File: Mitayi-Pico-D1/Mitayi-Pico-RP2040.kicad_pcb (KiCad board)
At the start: 2 copper layers, 51 x 21 mm, 73 parts, among them J1 EXP8, J10 GND, J2 USB-C-2.0, J3 Header-1, J4 Header-2, J5 SWD, J7 VBUS, J8 DM, J9 DP, SW1 UK-B0273-SP25Y, SW2 UK-B0273-SP25Y, U1 W25Q32JVSSIQ, U2 MIC5219-3.3YM5, U3 RP2040, Y1 YIC-12M20P2/XT324-10/10

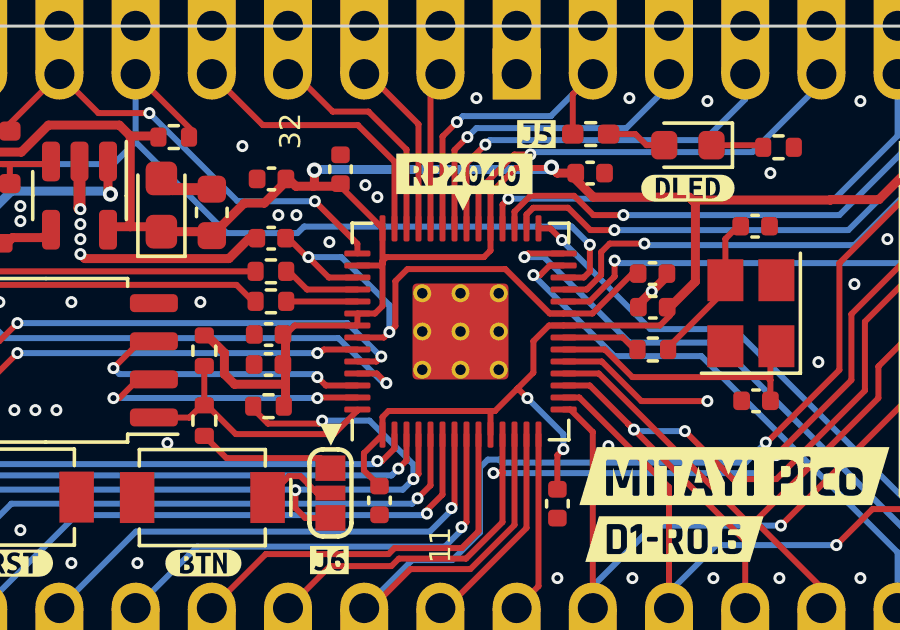
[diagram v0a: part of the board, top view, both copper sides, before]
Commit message: Updated `runDRC()`
- Updated `runDRC()`.
  - It now checks how many voilations were found in the DRC report and print them.
  - If violations are found, the user will be prompted to continue or exit the app.
  - The export log won't be saved if the user chooses to exit. The report will still be saved.
  - `pcb_drc` command execcution will be set to false if the user chooses to continue with DRC errors.
- New Version 🆕 `0.1.7`.
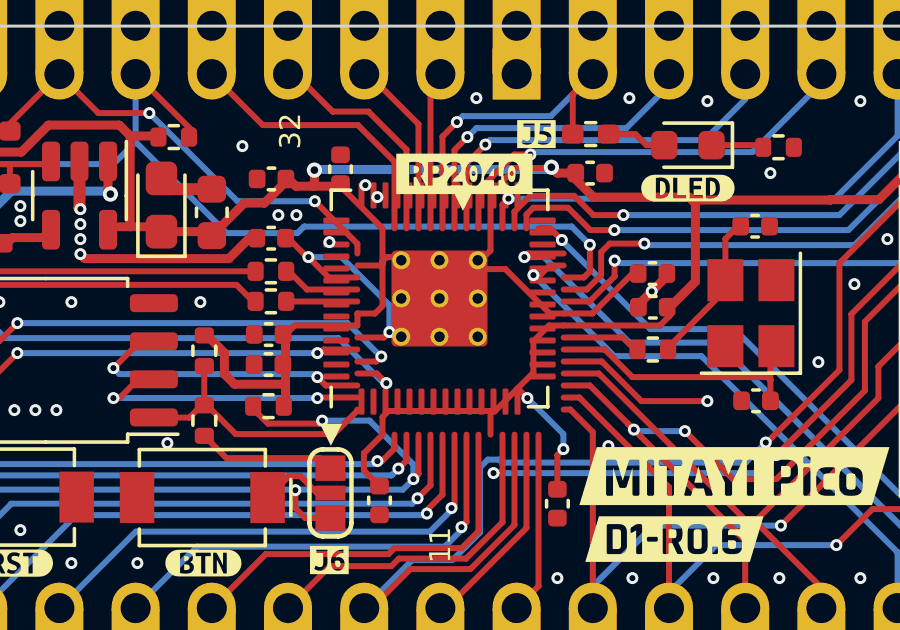
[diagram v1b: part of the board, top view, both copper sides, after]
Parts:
- moved U3 1.30 mm to (148.2, 87.9)

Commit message: Udpated
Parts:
- moved U3 4.60 mm to (151.6, 84.8)

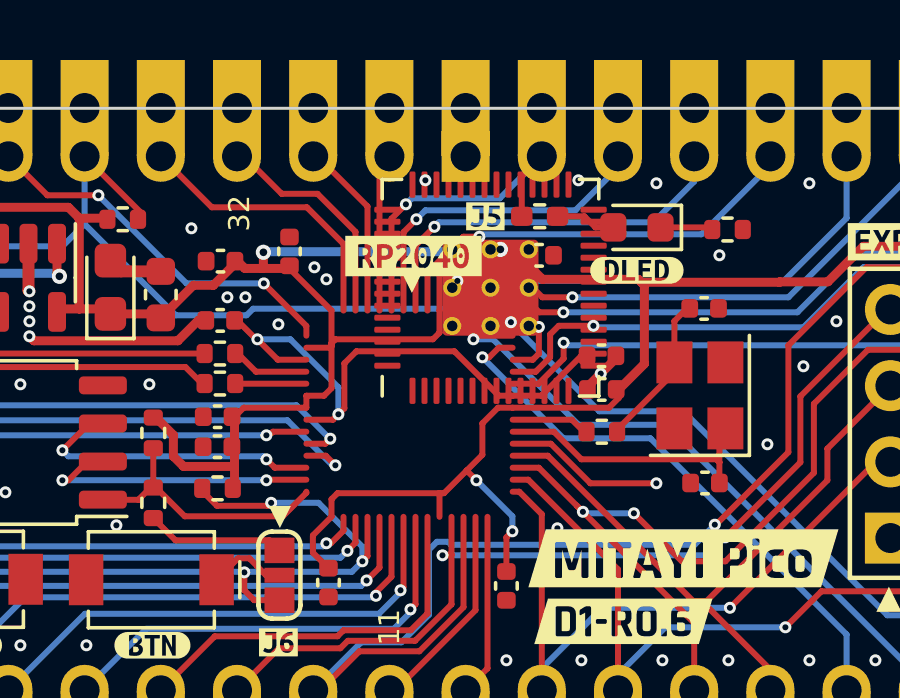
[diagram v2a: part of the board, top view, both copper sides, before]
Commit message: Added new options for the `bom` export command
- Added new options for the `bom` export command.
  - Added `--include-excluded-from-bom`.
- Added new options for the `sch_pdf` command.
  - Added `--default-font`.
  - Added `--exclude-pdf-hierarchical-links`.
  - Added `--exclude-pdf-metadata`.
- Added new options for the `pcb_pdf` command.
  - Added `--subtract-soldermask`.
  - Added `--sketch-pads-on-fab-layers`.
  - Added `--hide-DNP-footprints-on-fab-layers`.
  - Added `--sketch-DNP-footprints-on-fab-layers`.
  - Added `--crossout-DNP-footprints-on-fab-layers`.
  - Added `--plot-invisible-text`.
- Added new options for the `svg` command.
  - Added `--sketch-pads-on-fab-layers`.
  - Added `--hide-DNP-footprints-on-fab-layers`.
  - Added `--sketch-DNP-footprints-on-fab-layers`.
  - Added `--crossout-DNP-footprints-on-fab-layers`.
  - Added `--fit-page-to-board`.
  - Added `--plot-invisible-text`.
- In `generatePositions()`, the files are named with "Position" instead of "Pos".
- There will be a few breaking changes added to the upcoming versions as we need to add some functionalities that are now natively supported by KiCad CLI.
  - These changes will replace existing KiExport configuration parameters.
  - New version of KiExport will not support the older parameters.
  - The idea is to add support for as many new non-breaking command options as possible before the breaking changes are introduced.
- New Version 🆕 `0.1.12`.
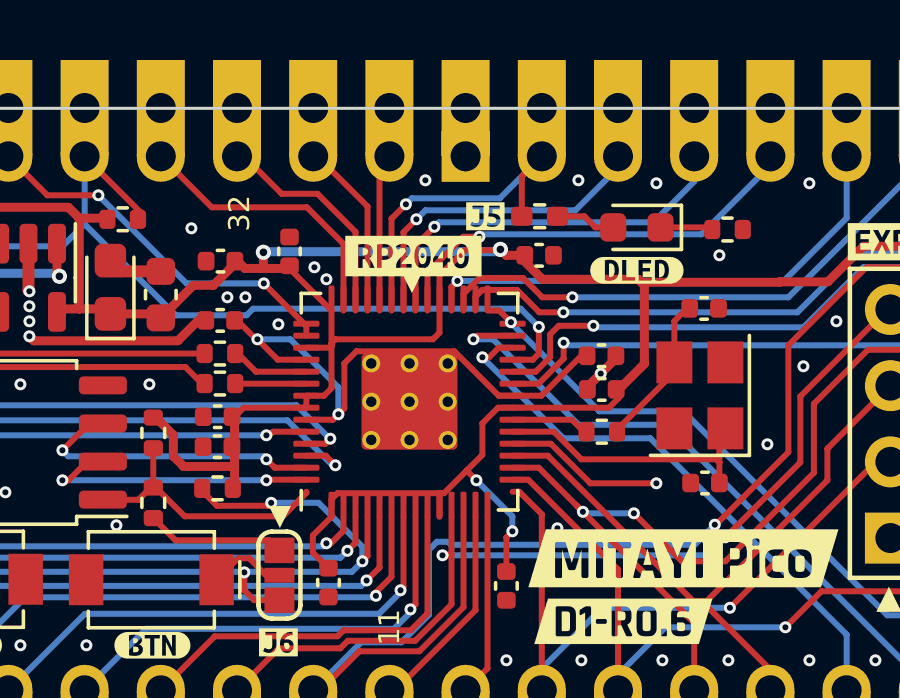
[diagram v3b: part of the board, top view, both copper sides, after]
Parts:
- moved U3 4.66 mm to (148.9, 88.6)
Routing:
- net /GPIO15: track 22.1 -> 27.4 mm
- net GND: track 21.0 -> 15.6 mm

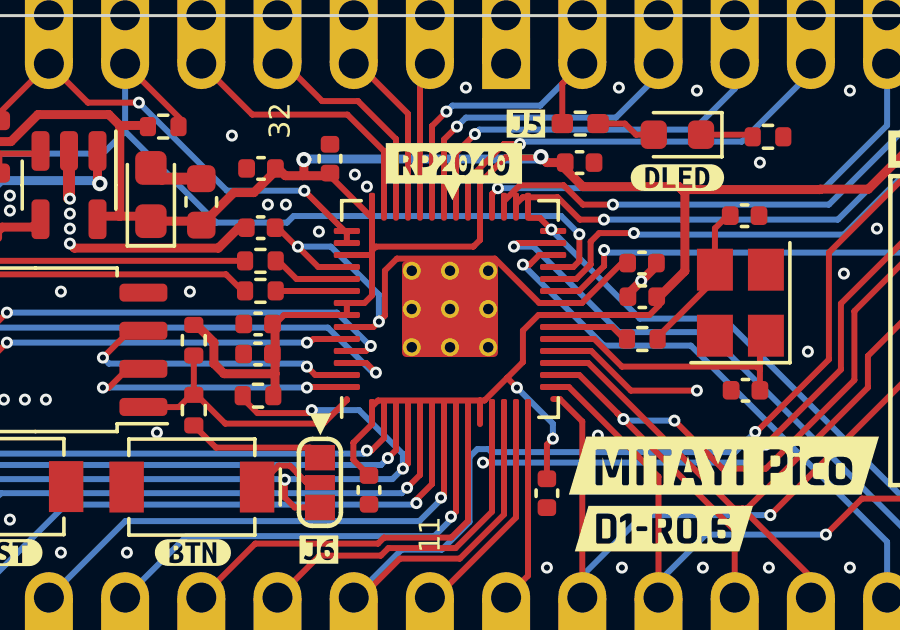
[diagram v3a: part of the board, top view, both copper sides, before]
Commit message: Added support for exporting rendered SVG images
- Added support for exporting rendered SVG images.
  - Updated the `kiexport.json` specification.
    - Updated the JSON version to `1.8`.
    - Added `vtracer_path`.
      - This tells where the VTracer SVG converter is located.
      - This can be a full path or jus the executable name if it is in the System Path.
    - Added `kie_generate_svg`.
      - This tells if an SVG should be generated from the rendered PNG images.
      - Can be `true` or `false`.
    - Added `kie_vtracer_params`.
      - This is a dictionary that holds all of the VTracer parameters.
  - Updated `MIN_CONFIG_JSON_VERSION` to `1.8`.
  - Updated `DEFAULT_CONFIG_JSON`.
  - Updated `LazyDict` callback.
    - The call will now return `None` when the key/value is not found.
    - We can then do a None check to find any missing keys/values.
  - Added `cropImage()`
    - Rendered images are cropped to remove empty spaces before converting to SVG.
- Added `pillow` to `requirements.txt`.
- New Version 🆕 `0.1.13`.
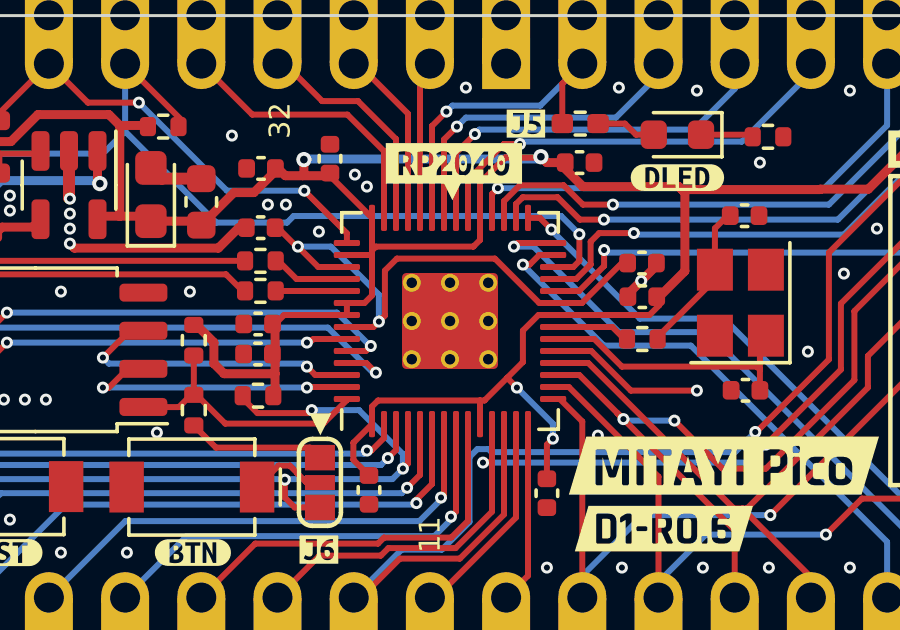
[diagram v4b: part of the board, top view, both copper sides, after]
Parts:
- moved U3 0.40 mm to (148.9, 89.0)
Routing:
- net /GPIO15: track 27.4 -> 22.1 mm
- net GND: track 15.6 -> 21.0 mm
